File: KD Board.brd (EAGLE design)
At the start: 42.8 x 34 mm, 10 parts, among them IC1 LM555D

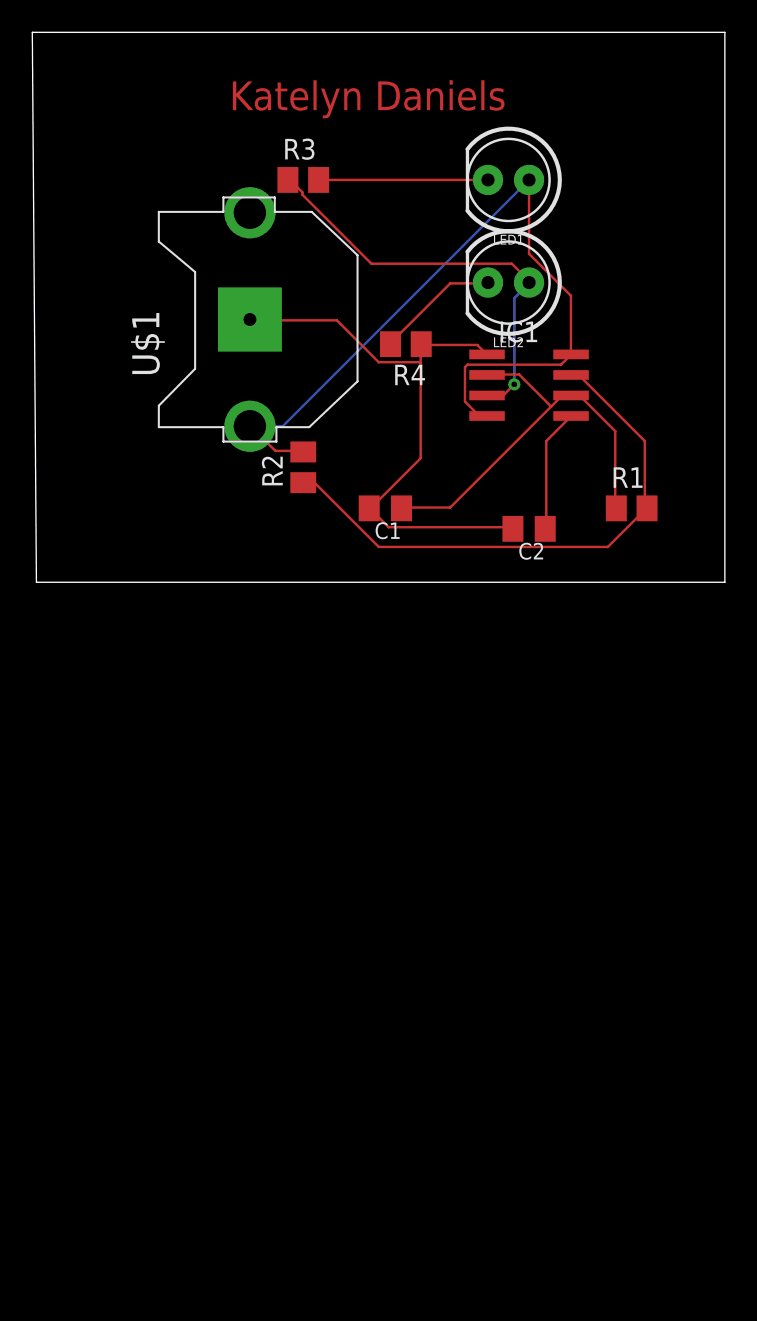
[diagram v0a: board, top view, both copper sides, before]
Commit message: Moved name to silk layer. Board not square. Minor fixes.
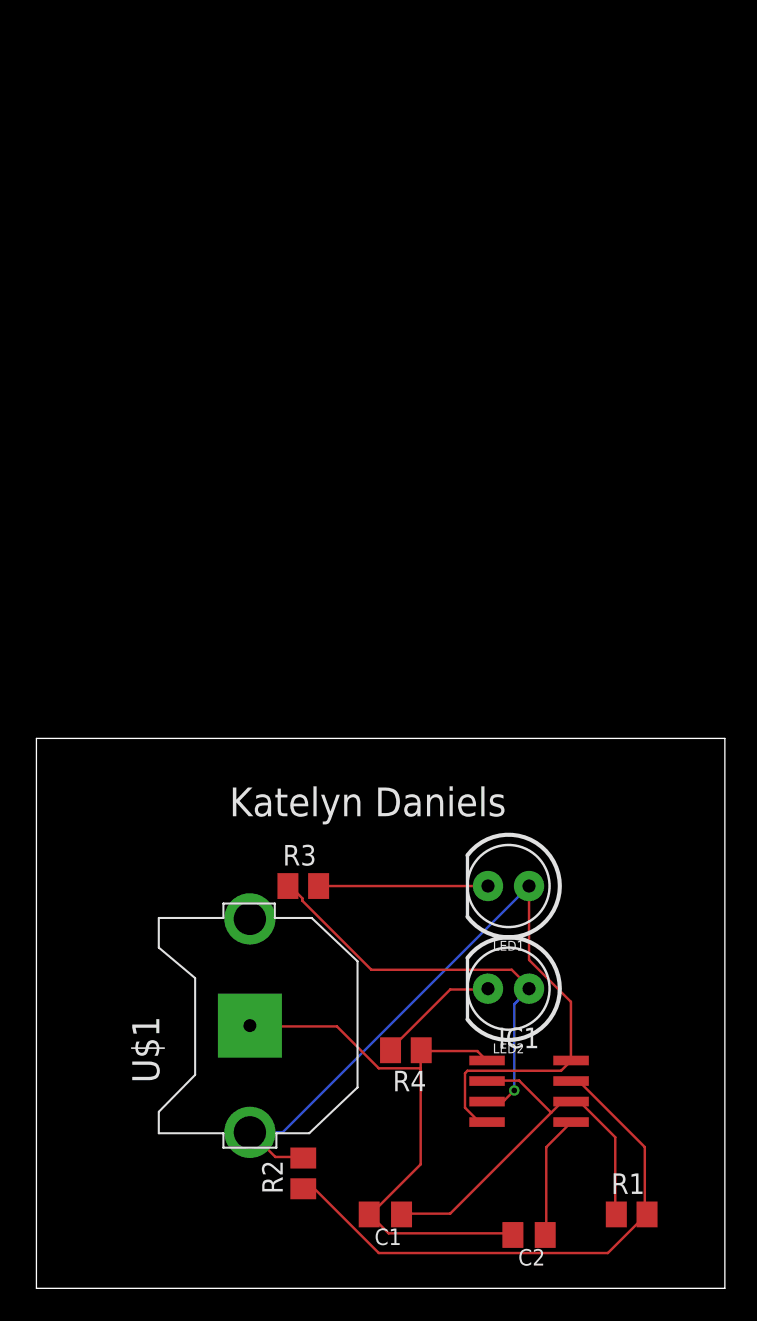
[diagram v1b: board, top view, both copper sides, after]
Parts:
- moved C2 43.7 mm to (30.5, 3.30)
- moved IC1 43.7 mm to (30.5, 12.2)
- moved LED1 43.7 mm to (29.2, 24.9)
- moved R3 43.7 mm to (16.5, 24.9)
- moved R4 43.7 mm to (22.9, 14.7)
- moved U$1 43.7 mm to (13.2, 16.3)
- moved C1 43.7 mm to (21.6, 4.57)
- moved LED2 43.7 mm to (29.2, 18.5)
- moved R1 43.7 mm to (36.8, 4.57)
- moved R2 43.7 mm to (16.5, 7.11)
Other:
- board size 42.8 x 34 mm -> 42.6 x 34 mm
